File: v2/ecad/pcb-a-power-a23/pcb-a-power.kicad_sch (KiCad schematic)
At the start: 391 parts, among them Q1 2N7002: panel controller high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, Q10 CSD18510Q5B 40 V N-FET, Q11 CSD18510Q5B 40 V N-FET, Q12 CSD18510Q5B 40 V N-FET, Q13 CSD18510Q5B 40 V N-FET, Q14 CSD18510Q5B 40 V N-FET, Q15 CSD18510Q5B 40 V N-FET, Q16 CSD18510Q5B 40 V N-FET, Q17 CSD19532Q5B 100 V N-FET (4.6 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, Q18 CSD19532Q5B 100 V N-FET (4.6 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, Q19 CSD19532Q5B 100 V N-FET (4.6 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, Q2 CSD19532Q5B 100 V N-FET (4.6 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, Q20 CSD19532Q5B 100 V N-FET (4.6 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, Q21 CSD18510Q5B 40 V N-FET, Q22 CSD18510Q5B 40 V N-FET, Q23 CSD18510Q5B 40 V N-FET, Q24 CSD18510Q5B 40 V N-FET, Q25 CSD18510Q5B 40 V N-FET, Q26 CSD18510Q5B 40 V N-FET, Q27 CSD18510Q5B 40 V N-FET (VBUS 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, Q3 CSD19532Q5B 100 V N-FET (4.6 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, Q4 CSD19532Q5B 100 V N-FET (4.6 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, Q5 CSD19532Q5B 100 V N-FET (4.6 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, Q6 2N7002: CHG_INHIBIT high = IL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, Q7 CSD18510Q5B 40 V N-FET, Q8 CSD18510Q5B 40 V N-FET, Q9 CSD18510Q5B 40 V N-FET, U1 LTC2954CTS8-1 push-button on/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, U10 INA226 rail monitor +5V_S3, U11 INA226 rail monitor +5V_DEV, U12 TPS62933DRLR 3 A buck, 3.3 V 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, U13 LM5176PWPR buck-boost control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, U14 INA226 PA rail monitor (0x46), U15 LM5176PWPR buck-boost control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, U16 LM5176PWPR buck-boost control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, U17 INA226 PoE rail monitor (0x47), U18 TPS25740ARGER USB-C PD source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, U19 LM5176PWPR buck-boost control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, U2 LM5176PWPR buck-boost control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, U21 TPS259631DDAR eFuse VBAT -> V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, U22 TPS259631DDAR eFuse VBAT -> V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, U23 TPS259631DDAR eFuse +5V_DEV -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, U26 SN74LVC08APWR quad AND: EMCON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, U27 PCA9555PW (0x21): enables and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, U28 PCA9555PW (0x24): power-good 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, U29 USBLC6-2SC6, U3 BQ25731RSNR 1 to 5 cell buck-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, U4 AP64500SP-13 5 A buck, 5.1 V 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, U5 AP64500SP-13 5 A buck, 5.1 V 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, U6 AP64500SP-13 5 A buck, 5.1 V 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, U7 AP64500SP-13 5 A buck, 5.1 V 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, U8 INA226 rail monitor +5V_S1, U9 INA226 rail monitor +5V_S2

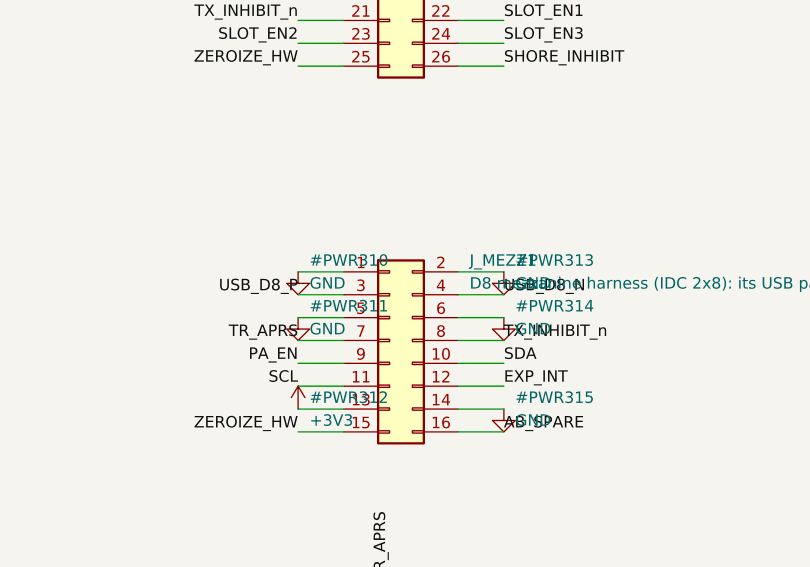
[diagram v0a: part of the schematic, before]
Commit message: fix(a): A's schematic regenerated for the harness pin map, and the contract passes again [MESHSAT-862]
check_contracts compares J_MEZZ1 (A) with J_HARN1 (D) pin for pin and refused
D's finish while A's netlist still carried the old map: differs on pins
1, 2, 3, 4. The gate is doing what it is for. With A's schematic regenerated
the whole set reads ALL CONTRACTS PASS, 40 of 40.
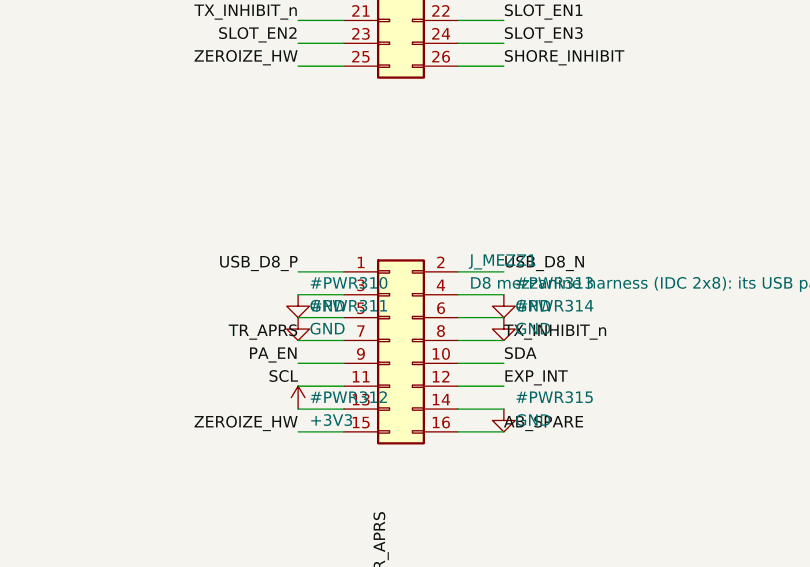
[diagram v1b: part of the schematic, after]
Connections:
- net GND: now also J_MEZZ1.3 (Pin_3), J_MEZZ1.4 (Pin_4); no longer J_MEZZ1.1 (Pin_1), J_MEZZ1.2 (Pin_2)
- net USB_D8_N: now also J_MEZZ1.2 (Pin_2); no longer J_MEZZ1.4 (Pin_4)
- net USB_D8_P: now also J_MEZZ1.1 (Pin_1); no longer J_MEZZ1.3 (Pin_3)
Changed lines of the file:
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@@
 	)
 	(wire (pts (xy 2410.46 359.41) (xy 2405.38 359.41)) (stroke (width 0) (type default)))
-	(symbol (lib_id "power:GND") (at 2405.38 359.41 0) (unit 1) (exclude_from_sim no) (in_bom no) (on_board no) (dnp no) (fields_autoplaced yes)
-		(property "Reference" "#PWR310" (at 2406.65 358.14 0) (effects (font (size 1.27 1.27)) (justify left)))
-		(property "Value" "GND" (at 2406.65 360.68 0) (effects (font (size 1.27 1.27)) (justify left)))
-		(property "Footprint" "" (at 2405.38 359.41 0) (effects (font (size 1.27 1.27)) (justify left) (hide yes)))
-		(property "Datasheet" "" (at 2405.38 359.41 0) (effects (font (size 1.27 1.27)) (justify left) (hide yes)))
-		(property "Description" "" (at 2405.38 359.41 0) (effects (font (size 1.27 1.27)) (justify left) (hide yes)))
+	(label "USB_D8_P" (at 2405.38 359.41 180) (fields_autoplaced yes) (effects (font (size 1.27 1.27)) (justify right bottom)))
+	(wire (pts (xy 2410.46 361.95) (xy 2405.38 361.95)) (stroke (width 0) (type default)))
+	(symbol (lib_id "power:GND") (at 2405.38 361.95 0) (unit 1) (exclude_from_sim no) (in_bom no) (on_board no) (dnp no) (fields_autoplaced yes)
+		(property "Reference" "#PWR310" (at 2406.65 360.68 0) (effects (font (size 1.27 1.27)) (justify left)))
+		(property "Value" "GND" (at 2406.65 363.22 0) (effects (font (size 1.27 1.27)) (justify left)))
+		(property "Footprint" "" (at 2405.38 361.95 0) (effects (font (size 1.27 1.27)) (justify left) (hide yes)))
+		(property "Datasheet" "" (at 2405.38 361.95 0) (effects (font (size 1.27 1.27)) (justify left) (hide yes)))
+		(property "Description" "" (at 2405.38 361.95 0) (effects (font (size 1.27 1.27)) (justify left) (hide yes)))
 		(pin "1")
 		(instances (project "pcb-a-power" (path "/5663fbcf-143d-5acc-8e65-3ad892df2ec3" (reference "#PWR310") (unit 1))))
 	)
-	(wire (pts (xy 2410.46 361.95) (xy 2405.38 361.95)) (stroke (width 0) (type default)))
-	(label "USB_D8_P" (at 2405.38 361.95 180) (fields_autoplaced yes) (effects (font (size 1.27 1.27)) (justify right bottom)))
 	(wire (pts (xy 2410.46 364.49) (xy 2405.38 364.49)) (stroke (width 0) (type default)))
 	(symbol (lib_id "power:GND") (at 2405.38 364.49 0) (unit 1) (exclude_from_sim no) (in_bom no) (on_board no) (dnp no) (fields_autoplaced yes)
@@
 	(label "ZEROIZE_HW" (at 2405.38 377.19 180) (fields_autoplaced yes) (effects (font (size 1.27 1.27)) (justify right bottom)))
 	(wire (pts (xy 2423.16 359.41) (xy 2428.24 359.41)) (stroke (width 0) (type default)))
-	(symbol (lib_id "power:GND") (at 2428.24 359.41 0) (unit 1) (exclude_from_sim no) (in_bom no) (on_board no) (dnp no) (fields_autoplaced yes)
-		(property "Reference" "#PWR313" (at 2429.51 358.14 0) (effects (font (size 1.27 1.27)) (justify left)))
-		(property "Value" "GND" (at 2429.51 360.68 0) (effects (font (size 1.27 1.27)) (justify left)))
-		(property "Footprint" "" (at 2428.24 359.41 0) (effects (font (size 1.27 1.27)) (justify left) (hide yes)))
-		(property "Datasheet" "" (at 2428.24 359.41 0) (effects (font (size 1.27 1.27)) (justify left) (hide yes)))
-		(property "Description" "" (at 2428.24 359.41 0) (effects (font (size 1.27 1.27)) (justify left) (hide yes)))
+	(label "USB_D8_N" (at 2428.24 359.41 0) (fields_autoplaced yes) (effects (font (size 1.27 1.27)) (justify left bottom)))
+	(wire (pts (xy 2423.16 361.95) (xy 2428.24 361.95)) (stroke (width 0) (type default)))
+	(symbol (lib_id "power:GND") (at 2428.24 361.95 0) (unit 1) (exclude_from_sim no) (in_bom no) (on_board no) (dnp no) (fields_autoplaced yes)
+		(property "Reference" "#PWR313" (at 2429.51 360.68 0) (effects (font (size 1.27 1.27)) (justify left)))
+		(property "Value" "GND" (at 2429.51 363.22 0) (effects (font (size 1.27 1.27)) (justify left)))
+		(property "Footprint" "" (at 2428.24 361.95 0) (effects (font (size 1.27 1.27)) (justify left) (hide yes)))
+		(property "Datasheet" "" (at 2428.24 361.95 0) (effects (font (size 1.27 1.27)) (justify left) (hide yes)))
+		(property "Description" "" (at 2428.24 361.95 0) (effects (font (size 1.27 1.27)) (justify left) (hide yes)))
 		(pin "1")
 		(instances (project "pcb-a-power" (path "/5663fbcf-143d-5acc-8e65-3ad892df2ec3" (reference "#PWR313") (unit 1))))
 	)
-	(wire (pts (xy 2423.16 361.95) (xy 2428.24 361.95)) (stroke (width 0) (type default)))
-	(label "USB_D8_N" (at 2428.24 361.95 0) (fields_autoplaced yes) (effects (font (size 1.27 1.27)) (justify left bottom)))
 	(wire (pts (xy 2423.16 364.49) (xy 2428.24 364.49)) (stroke (width 0) (type default)))
 	(symbol (lib_id "power:GND") (at 2428.24 364.49 0) (unit 1) (exclude_from_sim no) (in_bom no) (on_board no) (dnp no) (fields_autoplaced yes)

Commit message: feat(a): A's pre-route board with all three pairs laid and 0 hard [MESHSAT-862]
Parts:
- added J_AB2: A-B wall-port ribbon (IDC 2x5): the wall USB pair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, meshsat:IDC-Header_2x05_P2.54mm_Vertical_NarrowPad, symbol Connector_Generic:Conn_02x05_Odd_Even
- J_AB1: footprint Connector_IDC:IDC-Header_2x13_P2.54mm_Vertical -> meshsat:IDC-Header_2x13_P2.54mm_Vertical_NarrowPad
- J_MEZZ1: footprint Connector_IDC:IDC-Header_2x08_P2.54mm_Vertical -> meshsat:IDC-Header_2x08_P2.54mm_Vertical_NarrowPad
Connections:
- net EMCON_HW: now also J_AB1.15 (Pin_15); no longer J_AB1.20 (Pin_20)
- net EXP_INT: now also J_AB1.13 (Pin_13); no longer J_AB1.18 (Pin_18)
- net GND: now also J_AB1.22 (Pin_22), J_AB1.23 (Pin_23), J_AB1.24 (Pin_24), J_AB1.3 (Pin_3), J_AB1.4 (Pin_4), J_AB1.7 (Pin_7), J_AB1.8 (Pin_8), J_AB2.10 (Pin_10), J_AB2.3 (Pin_3), J_AB2.4 (Pin_4), J_AB2.5 (Pin_5), J_AB2.6 (Pin_6), J_AB2.7 (Pin_7), J_AB2.8 (Pin_8), J_AB2.9 (Pin_9); no longer J_AB1.1 (Pin_1), J_AB1.10 (Pin_10), J_AB1.13 (Pin_13), J_AB1.2 (Pin_2), J_AB1.9 (Pin_9)
- net PI_KILL: now also J_AB1.10 (Pin_10); no longer J_AB1.15 (Pin_15)
- net PI_SHDN_REQ: now also J_AB1.9 (Pin_9); no longer J_AB1.14 (Pin_14)
- net SCL: now also J_AB1.12 (Pin_12); no longer J_AB1.17 (Pin_17)
- net SDA: now also J_AB1.11 (Pin_11); no longer J_AB1.16 (Pin_16)
- net SHORE_INHIBIT: now also J_AB1.21 (Pin_21); no longer J_AB1.26 (Pin_26)
- net SLOT_EN1: now also J_AB1.17 (Pin_17); no longer J_AB1.22 (Pin_22)
- net SLOT_EN2: now also J_AB1.18 (Pin_18); no longer J_AB1.23 (Pin_23)
- net SLOT_EN3: now also J_AB1.19 (Pin_19); no longer J_AB1.24 (Pin_24)
- net TR_APRS: now also J_AB1.14 (Pin_14); no longer J_AB1.19 (Pin_19)
- net TX_INHIBIT_n: now also J_AB1.16 (Pin_16); no longer J_AB1.21 (Pin_21)
- net USB_D8_N: now also J_AB1.2 (Pin_2); no longer J_AB1.4 (Pin_4)
- net USB_D8_P: now also J_AB1.1 (Pin_1); no longer J_AB1.3 (Pin_3)
- net USB_E6_N: now also J_AB1.26 (Pin_26); no longer J_AB1.8 (Pin_8)
- net USB_E6_P: now also J_AB1.25 (Pin_25); no longer J_AB1.7 (Pin_7)
- net USB_WALL_N: now also J_AB2.2 (Pin_2); no longer J_AB1.12 (Pin_12)
- net USB_WALL_P: now also J_AB2.1 (Pin_1); no longer J_AB1.11 (Pin_11)
- net ZEROIZE_HW: now also J_AB1.20 (Pin_20); no longer J_AB1.25 (Pin_25)

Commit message: feat(pcb-a): A24 is cut, with owner ruling 10's capacitors and no re-route [MESHSAT-862]
meshsat-pcb-a-revA-A24. The routed board is the committed one, sha256 7c73b407 before the text swap and
fcd09f4f after it, and the copper was compared item by item across the change: 5,212 tracks and vias
identical, every zone's filled area identical, every one of the 400 footprints in the same place and at
the same angle. Ruling 10 said no layout change and no re-route, and that is what the board shows.

  hard 0 of the fifteen types        unrouted 0
  check_pcb_a ALL PASS, 798 checks   netlist_board 2004 of 2004
  dc_drop 12 of 12 rails MET         impedance 3 of 3 pairs
  contracts ALL PASS                 verify_deliverable ALL PASS, 35 of 35

The BOM carries what the owner ruled: C596319 on the twenty-two 10 uF 50 V X7R 1210 and C5156756 on the
three 10 uF 100 V parts of the PoE stage's output. 24 of 146 lines are blank and every one of them is
declared in the board's own lcsc-allow.txt with its reason.

Thirty-one references changed and none of them is copper: the twenty-five capacitors, three eFuse ILM
resistors that carried a CURRENT as their value and now carry the resistance TPS2596 equation 7 gives,
and three connector rows that named the lead instead of the socket.
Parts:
- C108, C109, C11, C110, C111, C116, C117, C118, C119, C12, C13, C14, C15, C63, C64, C65, C66, C67, C74, C81, C82, C92: value 22u 50V X7R 1210 -> 10u 50V X7R 1210
- C83, C84, C85: value 22u 50V X7R 1210 -> 10u 100V X7R 1210
- J_54V, J_5V_DEV, J_5V_S1, J_5V_S2, J_5V_S3, J_HF, J_MEZZ_PWR1, J_MON, J_PA: LCSC (none) -> C274411
- J_HEAT: value heater mat under the 2590 cradle (XH2.5): + - -> JST-XH 1x2 socket: the heater mat under the 2590 cradle, + and -; LCSC (none) -> C265283
- J_MAINSW: value MAIN button lead from the panel (XH2.5): PB, GND -> JST-XH 1x2 socket: the MAIN button lead from the panel, PB and GND; LCSC (none) -> C265283
- J_RF1, J_RF10, J_RF11, J_RF2, J_RF3, J_RF4, J_RF5, J_RF6, J_RF7, J_RF8, J_RF9: LCSC (none) -> C3174425
- J_USBW: value wall USB-C data pair to B16 passes here on the ribbon: this header is the pigtail's data side (D+ D- GND GND) -> JST-PH 1x4 socket: the wall USB-C data pair to B16 passes here on the ribbon, this is the pigtail's data side (D+ D- GN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; LCSC (none) -> C131334
- R90: value 1.2 A (ILM) -> 750R 1% (ILM: 1.2 A)
- R94: value 1.0 A (ILM) -> 909R 1% (ILM: 1.0 A)
- R98: value 2.0 A (ILM) -> 453R 1% (ILM: 2.0 A)
- U21: value TPS259631DDAR eFuse VBAT -> VMON (1.2 A (ILM)) -> TPS259631DDAR eFuse VBAT -> VMON (750R 1% (ILM: 1.2 A))
- U22: value TPS259631DDAR eFuse VBAT -> VHEAT (1.0 A (ILM)) -> TPS259631DDAR eFuse VBAT -> VHEAT (909R 1% (ILM: 1.0 A))
- U23: value TPS259631DDAR eFuse +5V_DEV -> +5V_D8 (2.0 A (ILM)) -> TPS259631DDAR eFuse +5V_DEV -> +5V_D8 (453R 1% (ILM: 2.0 A))
